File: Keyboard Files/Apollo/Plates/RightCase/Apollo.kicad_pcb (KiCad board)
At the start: 2 copper layers, 160.4 x 130.2 mm, 31 parts

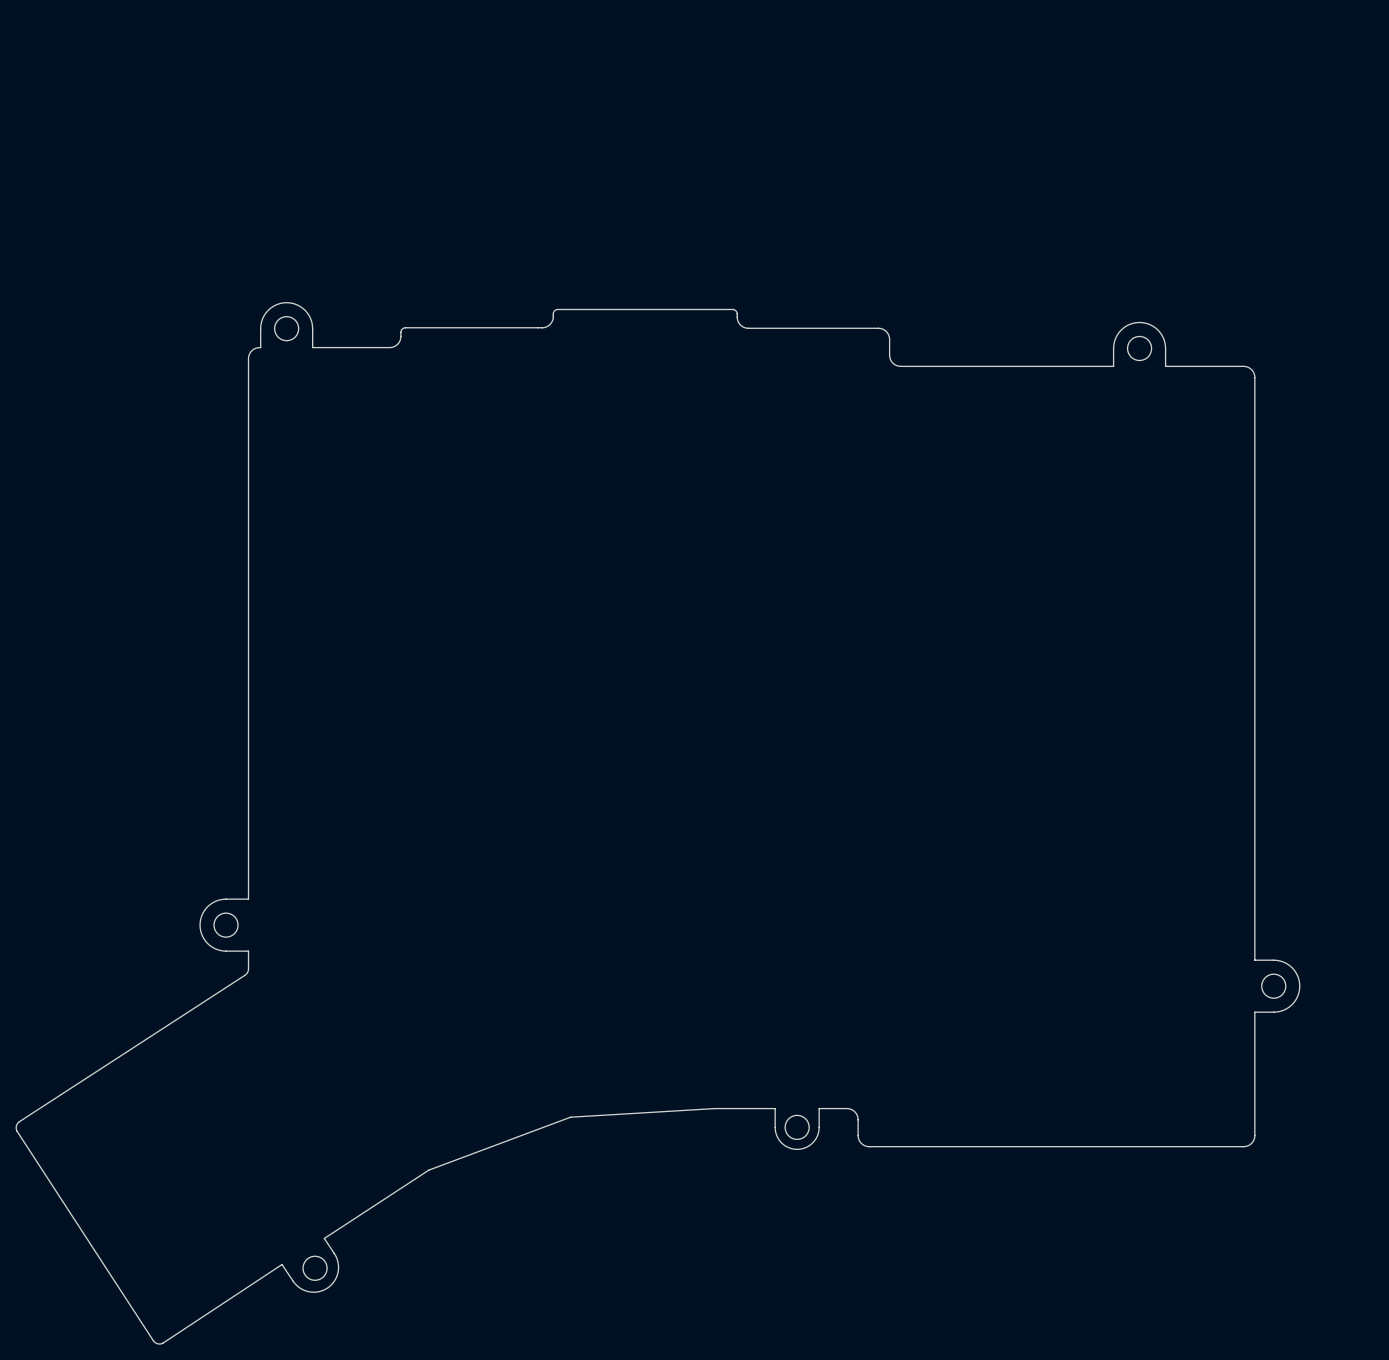
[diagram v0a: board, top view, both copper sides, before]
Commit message: Increase Apollo plate bezel
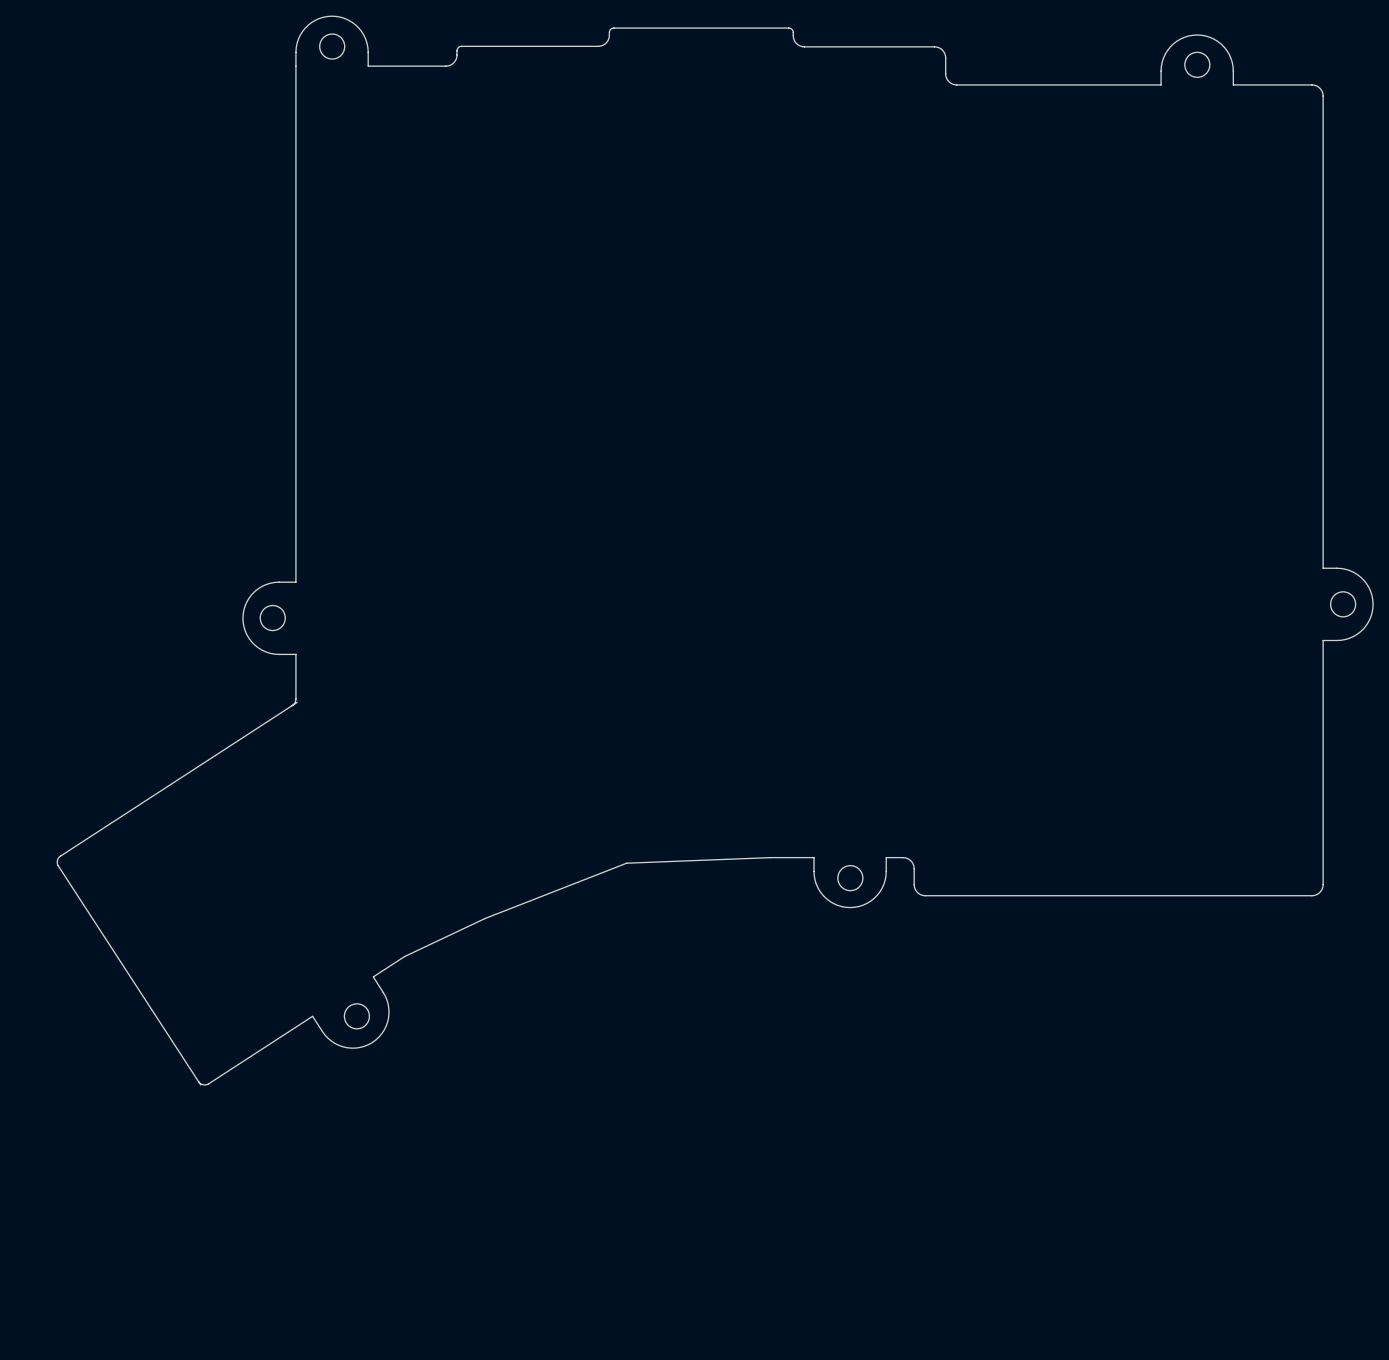
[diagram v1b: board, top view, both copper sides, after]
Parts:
- removed the REF** at (128.7, 99.4)
- removed the REF** at (145.9, 175.6)
- removed the REF** at (128.7, 156.5)
- removed the REF** at (128.7, 137.5)
- removed the REF** at (128.7, 118.4)
- removed the REF** at (147.8, 154.1)
- removed the REF** at (147.8, 135.1)
- removed the REF** at (147.8, 97.0)
- removed the REF** at (147.8, 116.0)
- removed the REF** at (166.8, 94.6)
- removed the REF** at (166.8, 113.7)
- removed the REF** at (166.8, 151.8)
- removed the REF** at (166.8, 132.7)
- removed the REF** at (204.9, 101.7)
- removed the REF** at (204.9, 120.8)
- removed the REF** at (204.9, 177.9)
- removed the REF** at (204.9, 158.9)
- removed the REF** at (204.9, 139.8)
- removed the REF** at (106.6, 193.5)
- removed the REF** at (122.5, 183.2)
- added REF**: MX_Switch_Cutout, Keebio-Parts:MX_Switch_Cutout, B.Cu at (135.7, 66.1)
- added REF**: MX_Switch_Cutout, Keebio-Parts:MX_Switch_Cutout, B.Cu at (152.9, 142.4)
- added REF**: MX_Switch_Cutout, Keebio-Parts:MX_Switch_Cutout, B.Cu at (135.7, 123.3)
- added REF**: MX_Switch_Cutout, Keebio-Parts:MX_Switch_Cutout, B.Cu at (135.7, 104.2)
- added REF**: MX_Switch_Cutout, Keebio-Parts:MX_Switch_Cutout, B.Cu at (135.7, 85.2)
- added REF**: MX_Switch_Cutout, Keebio-Parts:MX_Switch_Cutout, B.Cu at (154.8, 120.8)
- added REF**: MX_Switch_Cutout, Keebio-Parts:MX_Switch_Cutout, B.Cu at (154.8, 101.8)
- added REF**: MX_Switch_Cutout, Keebio-Parts:MX_Switch_Cutout, B.Cu at (154.8, 63.7)
- added REF**: MX_Switch_Cutout, Keebio-Parts:MX_Switch_Cutout, B.Cu at (154.8, 82.7)
- added REF**: MX_Switch_Cutout, Keebio-Parts:MX_Switch_Cutout, B.Cu at (173.8, 61.3)
- added REF**: MX_Switch_Cutout, Keebio-Parts:MX_Switch_Cutout, B.Cu at (173.8, 80.4)
- added REF**: MX_Switch_Cutout, Keebio-Parts:MX_Switch_Cutout, B.Cu at (173.8, 118.5)
- added REF**: MX_Switch_Cutout, Keebio-Parts:MX_Switch_Cutout, B.Cu at (173.8, 99.4)
- added REF**: MX_Switch_Cutout, Keebio-Parts:MX_Switch_Cutout, B.Cu at (211.9, 68.5)
- added REF**: MX_Switch_Cutout, Keebio-Parts:MX_Switch_Cutout, B.Cu at (211.9, 87.5)
- added REF**: MX_Switch_Cutout, Keebio-Parts:MX_Switch_Cutout, B.Cu at (211.9, 144.7)
- added REF**: MX_Switch_Cutout, Keebio-Parts:MX_Switch_Cutout, B.Cu at (211.9, 125.6)
- added REF**: MX_Switch_Cutout, Keebio-Parts:MX_Switch_Cutout, B.Cu at (211.9, 106.6)
- added REF**: MX_Switch_Cutout, Keebio-Parts:MX_Switch_Cutout, B.Cu at (113.6, 160.3)
- added REF**: MX_Switch_Cutout, Keebio-Parts:MX_Switch_Cutout, B.Cu at (129.5, 149.9)
- moved REF** 34.0 mm to (192.9, 101.8)
- moved REF** 34.0 mm to (235.7, 125.6)
- moved REF** 34.0 mm to (192.9, 63.7)
- moved REF** 34.0 mm to (173.8, 137.5)
- moved REF** 34.0 mm to (192.9, 139.9)
- moved REF** 34.0 mm to (235.7, 106.6)
- moved REF** 34.0 mm to (192.9, 82.7)
- moved REF** 34.0 mm to (235.7, 68.5)
- moved REF** 34.0 mm to (235.7, 144.7)
- moved REF** 34.0 mm to (235.7, 87.5)
- moved REF** 34.0 mm to (192.9, 120.8)
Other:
- board size 160.4 x 130.2 mm -> 164.5 x 133.6 mm
